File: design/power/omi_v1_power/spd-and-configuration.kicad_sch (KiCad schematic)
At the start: 2 parts

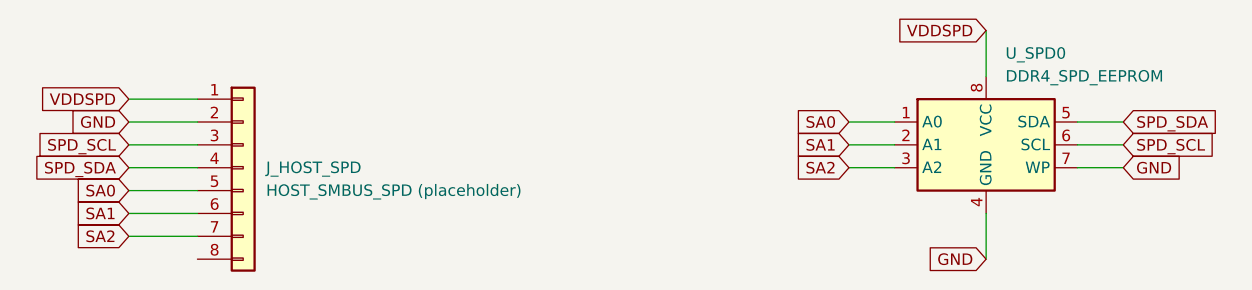
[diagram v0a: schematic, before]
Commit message: feat(phase3): remove redundant J_HOST_SPD placeholder connector
J1 now carries every SPD net (VDDSPD/GND/SPD_SCL/SPD_SDA/SA0-2), each verified
to still hold {J1, U_SPD0} after removal. Removed the symbol + its 7 pin global
labels + 7 wire stubs; U_SPD0 and its labels keep the nets. Not a jumper.
ERC 133 -> 132 (spd pin_not_connected 1 -> 0). No new dangling. Netlist parses.

Co-Authored-By: Claude Opus 4.8 (1M context) <noreply@anthropic.com>
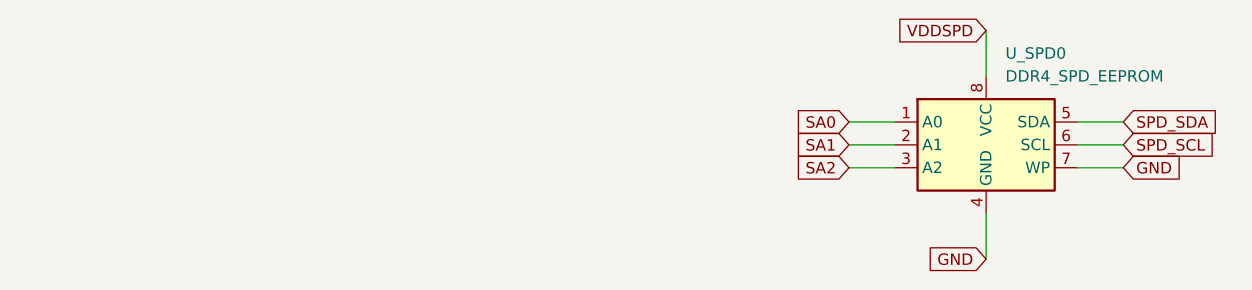
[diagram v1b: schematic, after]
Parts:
- removed J_HOST_SPD: HOST_SMBUS_SPD (placeholder), symbol Connector_Generic:Conn_01x08

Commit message: polish(schematic): v1.1.0 title blocks + sheet annotations (no electrical change)
Hand-done KiCad 9 GUI pass over all five schematic sheets. Title-block
and text-box content only — no wiring, no component, no net changes.

- Title block (all sheets): Company=OMI, Rev=1.1.0, Date=2026-06-02,
  plus functional per-sheet titles.
- Repurposed the previously-empty DQ/DQS sheet into a byte-lane reference table.
- Added a mechanical caveat text box on the edge (UDIMM) sheet.
- Added a power-rail summary text box on the root sheet.
- omi_v1_power.kicad_prl: project-local UI state saved with the GUI session.

Electrical integrity is asserted to be unchanged and is verified downstream
by the export pipeline (ERC=0 gate + byte-identical netlist and BOM).

Co-Authored-By: Claude Opus 4.8 (1M context) <noreply@anthropic.com>
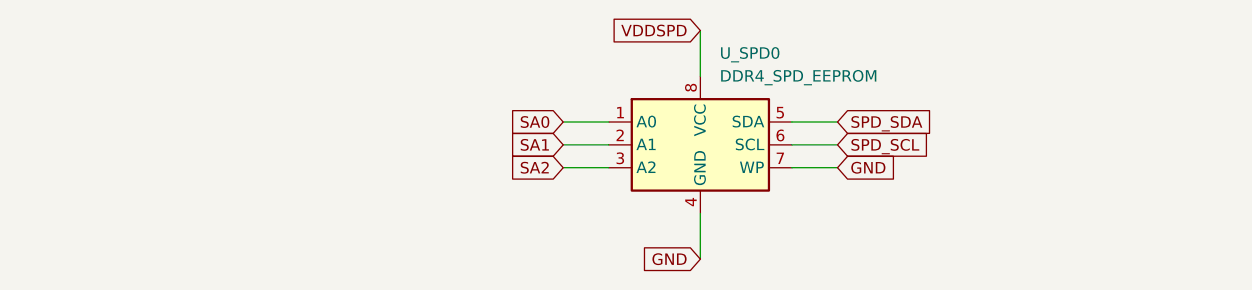
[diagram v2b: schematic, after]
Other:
- title: Stage 7.4 — SPD & Configuration -> SPD & Configuration
- moved on the sheet: U_SPD0
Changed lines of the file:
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@@
 	(paper "A4")
 	(title_block
-		(title "Stage 7.4 — SPD & Configuration")
-		(date "2026-02-27")
+		(title "SPD & Configuration")
+		(date "2026-06-02")
+		(rev "1.1.0")
 		(company "OMI")
 		(comment 3 "Assumptions:\n- SMBus pull-ups for SPD_SCL and SPD_SDA are provided by host platform.\n- WP is tied low (writes enabled) for OMI v1 development.\n- SA0/SA1/SA2 are slot/address straps (host-side).")
@@
 	(wire
 		(pts
-			(xy 179.07 93.98) (xy 184.15 93.98)
-		)
-		(stroke
-			(width 0)
-			(type default)
-		)
-	)
-	(wire
-		(pts
-			(xy 153.67 96.52) (xy 158.75 96.52)
-		)
-		(stroke
-			(width 0)
-			(type default)
-		)
-	)
-	(wire
-		(pts
-			(xy 168.91 83.82) (xy 168.91 88.9)
-		)
-		(stroke
-			(width 0)
-			(type default)
-		)
-	)
-	(wire
-		(pts
-			(xy 168.91 104.14) (xy 168.91 109.22)
-		)
-		(stroke
-			(width 0)
-			(type default)
-		)
-	)
-	(wire
-		(pts
-			(xy 153.67 93.98) (xy 158.75 93.98)
-		)
-		(stroke
-			(width 0)
-			(type default)
-		)
-	)
-	(wire
-		(pts
-			(xy 179.07 96.52) (xy 184.15 96.52)
-		)
-		(stroke
-			(width 0)
-			(type default)
-		)
-	)
-	(wire
-		(pts
-			(xy 179.07 99.06) (xy 184.15 99.06)
-		)
-		(stroke
-			(width 0)
-			(type default)
-		)
-	)
-	(wire
-		(pts
-			(xy 153.67 99.06) (xy 158.75 99.06)
+			(xy 147.32 93.98) (xy 152.4 93.98)
+		)
+		(stroke
+			(width 0)
+			(type default)
+		)
+	)
+	(wire
+		(pts
+			(xy 121.92 96.52) (xy 127 96.52)
+		)
+		(stroke
+			(width 0)
+			(type default)
+		)
+	)
+	(wire
+		(pts
+			(xy 137.16 83.82) (xy 137.16 88.9)
+		)
+		(stroke
+			(width 0)
+			(type default)
+		)
+	)
+	(wire
+		(pts
+			(xy 137.16 104.14) (xy 137.16 109.22)
+		)
+		(stroke
+			(width 0)
+			(type default)
+		)
+	)
+	(wire
+		(pts
+			(xy 121.92 93.98) (xy 127 93.98)
+		)
+		(stroke
+			(width 0)
+			(type default)
+		)
+	)
+	(wire
+		(pts
+			(xy 147.32 96.52) (xy 152.4 96.52)
+		)
+		(stroke
+			(width 0)
+			(type default)
+		)
+	)
+	(wire
+		(pts
+			(xy 147.32 99.06) (xy 152.4 99.06)
+		)
+		(stroke
+			(width 0)
+			(type default)
+		)
+	)
+	(wire
+		(pts
+			(xy 121.92 99.06) (xy 127 99.06)
 		)
 		(stroke
@@
 	(global_label "VDDSPD"
 		(shape input)
-		(at 168.91 83.82 180)
-		(fields_autoplaced yes)
-		(effects
-			(font
-				(size 1.27 1.27)
-			)
-			(justify right)
-		)
-		(property "Intersheetrefs" "${INTERSHEET_REFS}"
-			(at 158.5467 83.82 0)
+		(at 137.16 83.82 180)
+		(fields_autoplaced yes)
+		(effects
+			(font
+				(size 1.27 1.27)
+			)
+			(justify right)
+		)
+		(property "Intersheetrefs" "${INTERSHEET_REFS}"
+			(at 126.7967 83.82 0)
 			(effects
 				(font
@@
 	(global_label "SA0"
 		(shape input)
-		(at 153.67 93.98 180)
-		(fields_autoplaced yes)
-		(effects
-			(font
-				(size 1.27 1.27)
-			)
-			(justify right)
-		)
-		(property "Intersheetrefs" "${INTERSHEET_REFS}"
-			(at 147.1772 93.98 0)
+		(at 121.92 93.98 180)
+		(fields_autoplaced yes)
+		(effects
+			(font
+				(size 1.27 1.27)
+			)
+			(justify right)
+		)
+		(property "Intersheetrefs" "${INTERSHEET_REFS}"
+			(at 115.4272 93.98 0)
 			(effects
 				(font
@@
 	(global_label "SPD_SCL"
 		(shape input)
-		(at 184.15 96.52 0)
+		(at 152.4 96.52 0)
 		(fields_autoplaced yes)
 		(effects
@@
 		)
 		(property "Intersheetrefs" "${INTERSHEET_REFS}"
-			(at 195.3599 96.52 0)
+			(at 163.6099 96.52 0)
 			(effects
 				(font
@@
 	(global_label "GND"
 		(shape input)
-		(at 168.91 109.22 180)
-		(fields_autoplaced yes)
-		(effects
-			(font
-				(size 1.27 1.27)
-			)
-			(justify right)
-		)
-		(property "Intersheetrefs" "${INTERSHEET_REFS}"
-			(at 162.0543 109.22 0)
+		(at 137.16 109.22 180)
+		(fields_autoplaced yes)
+		(effects
+			(font
+				(size 1.27 1.27)
+			)
+			(justify right)
+		)
+		(property "Intersheetrefs" "${INTERSHEET_REFS}"
+			(at 130.3043 109.22 0)
 			(effects
 				(font
@@
 	(global_label "SPD_SDA"
 		(shape input)
-		(at 184.15 93.98 0)
+		(at 152.4 93.98 0)
 		(fields_autoplaced yes)
 		(effects
@@
 		)
 		(property "Intersheetrefs" "${INTERSHEET_REFS}"
-			(at 195.4204 93.98 0)
+			(at 163.6704 93.98 0)
 			(effects
 				(font
@@
 	(global_label "GND"
 		(shape input)
-		(at 184.15 99.06 0)
+		(at 152.4 99.06 0)
 		(fields_autoplaced yes)
 		(effects
@@
 		)
 		(property "Intersheetrefs" "${INTERSHEET_REFS}"
-			(at 191.0057 99.06 0)
+			(at 159.2557 99.06 0)
 			(effects
 				(font
@@
 	(global_label "SA1"
 		(shape input)
-		(at 153.67 96.52 180)
-		(fields_autoplaced yes)
-		(effects
-			(font
-				(size 1.27 1.27)
-			)
-			(justify right)
-		)
-		(property "Intersheetrefs" "${INTERSHEET_REFS}"
-			(at 147.1772 96.52 0)
+		(at 121.92 96.52 180)
+		(fields_autoplaced yes)
+		(effects
+			(font
+				(size 1.27 1.27)
+			)
+			(justify right)
+		)
+		(property "Intersheetrefs" "${INTERSHEET_REFS}"
+			(at 115.4272 96.52 0)
 			(effects
 				(font
@@
 	(global_label "SA2"
 		(shape input)
-		(at 153.67 99.06 180)
-		(fields_autoplaced yes)
-		(effects
-			(font
-				(size 1.27 1.27)
-			)
-			(justify right)
-		)
-		(property "Intersheetrefs" "${INTERSHEET_REFS}"
-			(at 147.1772 99.06 0)
+		(at 121.92 99.06 180)
+		(fields_autoplaced yes)
+		(effects
+			(font
+				(size 1.27 1.27)
+			)
+			(justify right)
+		)
+		(property "Intersheetrefs" "${INTERSHEET_REFS}"
+			(at 115.4272 99.06 0)
 			(effects
 				(font
@@
 	(symbol
 		(lib_id "Memory_EEPROM:AT24CS01-MAHM")
-		(at 168.91 96.52 0)
+		(at 137.16 96.52 0)
 		(unit 1)
 		(exclude_from_sim no)
@@
 		(fields_autoplaced yes)
 		(property "Reference" "U_SPD0"
-			(at 171.0533 86.36 0)
+			(at 139.3033 86.36 0)
 			(effects
 				(font
@@
 		)
 		(property "Value" "DDR4_SPD_EEPROM"
-			(at 171.0533 88.9 0)
+			(at 139.3033 88.9 0)
 			(effects
 				(font
@@
 		)
 		(property "Footprint" "Package_DFN_QFN:DFN-8-1EP_3x2mm_P0.5mm_EP1.3x1.5mm"
-			(at 168.91 96.52 0)
+			(at 137.16 96.52 0)
 			(effects
 				(font
@@
 		)
 		(property "Datasheet" "http://ww1.microchip.com/downloads/en/DeviceDoc/Atmel-8815-SEEPROM-AT24CS01-02-Datasheet.pdf"
-			(at 168.91 96.52 0)
+			(at 137.16 96.52 0)
 			(effects
 				(font
@@
 		)
 		(property "Description" "I2C Serial EEPROM, 1Kb (128x8) with Unique Serial Number, UDFN8"
-			(at 168.91 96.52 0)
+			(at 137.16 96.52 0)
 			(effects
 				(font
@@
 		)
 		(instances
-			(project ""
+			(project "omi_v1_power"
 				(path "/464309c0-e3ad-4428-a43f-e1cf3b7a7d42/32845847-1fe2-4b3a-b24a-3fdd7e5b4214"
 					(reference "U_SPD0")
